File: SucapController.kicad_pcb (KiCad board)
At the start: 2 copper layers, 39.2 x 30.4 mm, 44 parts, among them J2 , J4 Conn_02x03_Counter_Clockwise, J5 Conn_02x03_Counter_Clockwise, J6 Conn_02x03_Counter_Clockwise, Q1 SI2301, U1 HX9193-33GB, U10 TL431, U2 HX9193, U3 W25Q32JVSS, U4 STM32H750VBT6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

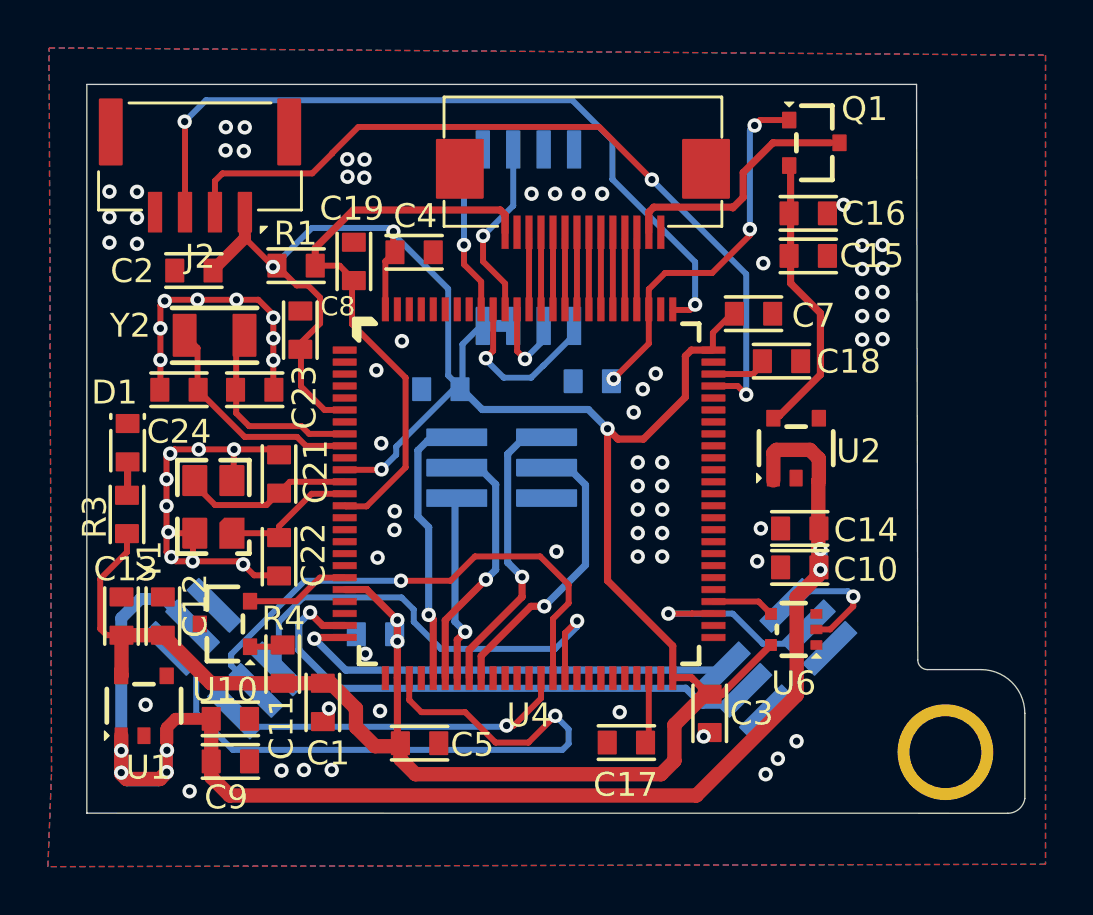
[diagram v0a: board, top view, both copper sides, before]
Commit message: fix some error of TL431
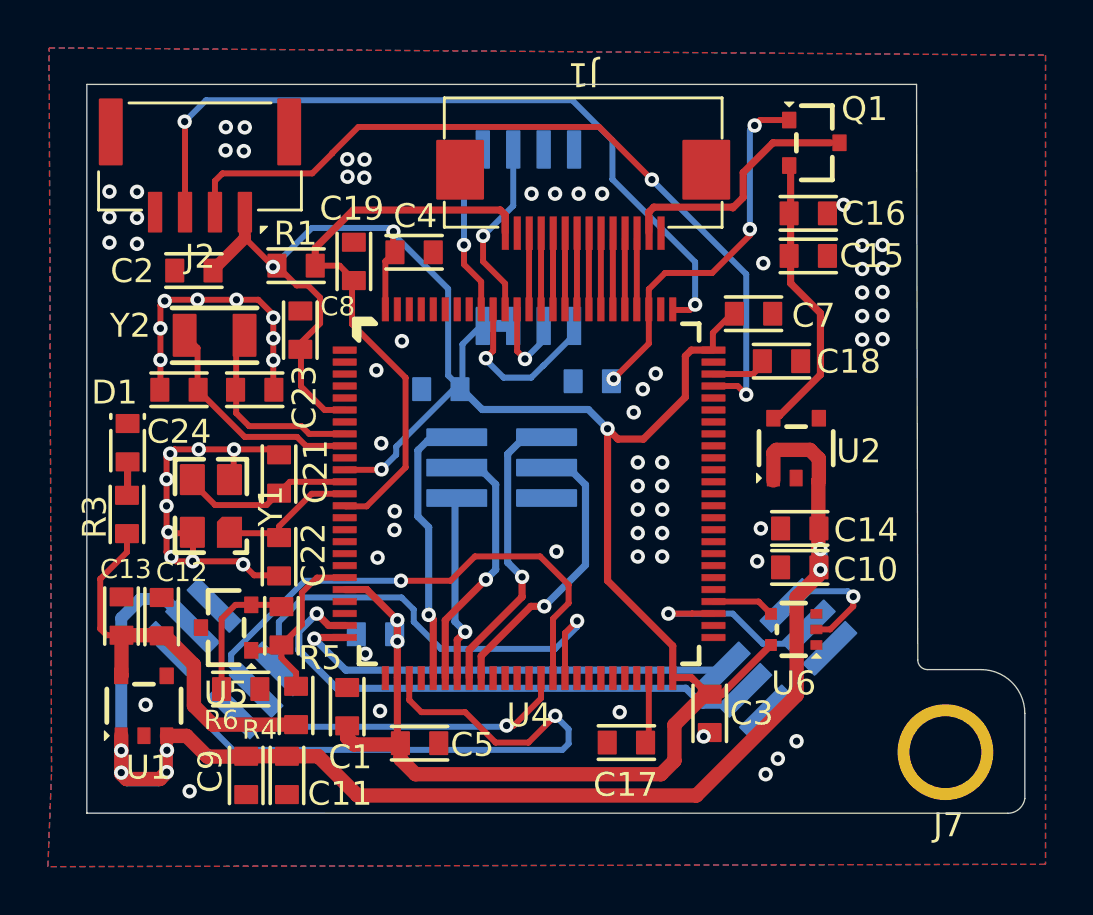
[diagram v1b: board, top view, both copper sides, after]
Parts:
- removed  : Conn_01x14, MECHANICAL_EDGE-CONN:FFC_14
- removed  : Screw_Terminal_01x01, GENERAL_HOLE:HOLE-04-03_1
- removed U10: TL431, GENERAL_SMALL-SEMI_SMD:SOT-23
- added J1: Conn_01x14, MECHANICAL_EDGE-CONN:FFC_14, F.Cu at (207.1, 86.1)
- added J7: Screw_Terminal_01x01, MECHANICAL:HOLE-04-03_1, F.Cu at (222.4, 110.7)
- added R5: 10k, GENERAL_RCL_SMD:R0603(1608M), F.Cu at (194.5, 105.5)
- added R6: 50k, GENERAL_RCL_SMD:R0603(1608M), F.Cu at (192.8, 108.1)
- added U5: TL431, GENERAL_SMALL-SEMI_SMD:SOT-23, F.Cu at (192.2, 105.5)
- R4: value Resistor -> 10k
- moved C11 3.34 mm to (194.7, 111.7), turned to 90 degrees
- moved R4 1.82 mm to (195.1, 108.8)
- moved C1 1.03 mm to (197.3, 108.8), turned to -90 degrees
- moved C9 0.88 mm to (193.0, 111.7), turned to 90 degrees
- moved Y1 0.11 mm to (191.6, 100.5)
- moved C12 0.06 mm to (189.5, 105.1)
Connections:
- R4 pad 2: Net-(R4-Pad2) -> /VREF
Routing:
- net Net-(R5-Pad1): track 0.00 -> 6.02 mm
- net /VREF: track 4.36 -> 7.92 mm
- net +5V: track 64.2 -> 62.0 mm
- net Net-(R4-Pad2): track 1.39 -> 0.00 mm
- net +3V3: track 119.2 -> 118.1 mm
- net GND: vias 82 -> 78

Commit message: fix some error
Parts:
-  : renamed from U5
-  : renamed from J2
-  : renamed from J1
-  : renamed from J7
-  : renamed from Y1
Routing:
- net +3V3: track 118.1 -> 120.2 mm
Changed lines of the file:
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@@
     (property "Sheetname" "")
     (attr smd)
-    (fp_text reference "U5" (at 0 2.75 unlocked) (layer "F.SilkS")
+    (fp_text reference " " (at 0 2.75 unlocked) (layer "F.SilkS")
       (effects (font (size 1 1) (thickness 0.15)))
     )
@@
     (property "Sheetname" "")
     (attr smd)
-    (fp_text reference "J2" (at 0 3.81 unlocked) (layer "F.SilkS")
+    (fp_text reference " " (at 0 3.81 unlocked) (layer "F.SilkS")
       (effects (font (size 1 1) (thickness 0.15)))
     )
@@
     (property "Sheetname" "")
     (attr smd)
-    (fp_text reference "J1" (at 0 3.683 180 unlocked) (layer "F.SilkS")
+    (fp_text reference " " (at 0 3.683 180 unlocked) (layer "F.SilkS")
       (effects (font (size 1 1) (thickness 0.15)))
     )
@@
     (property "Sheetname" "")
     (attr smd)
-    (fp_text reference "J7" (at 0 3.048 unlocked) (layer "F.SilkS")
+    (fp_text reference " " (at 0 3.048 unlocked) (layer "F.SilkS")
       (effects (font (size 1 1) (thickness 0.15)))
     )
@@
     (property "Sheetname" "")
     (attr smd)
-    (fp_text reference "Y1" (at 0 2.5 90 unlocked) (layer "F.SilkS")
+    (fp_text reference " " (at 0 2.5 90 unlocked) (layer "F.SilkS")
       (effects (font (size 1 1) (thickness 0.15)))
     )
@@
     (property "Sheetname" "")
     (attr smd)
-    (fp_text reference "R6" (at 0.8128 -1.2954) (layer "F.SilkS")
+    (fp_text reference "R6" (at 0.8128 -1.397) (layer "F.SilkS")
       (effects (font (size 0.8 0.8) (thickness 0.15)))
     )
@@
   (segment (start 212.2016 108.3184) (end 212.3948 108.3184) (width 0.6) (layer "F.Cu") (net 2))
   (segment (start 208.1276 97.2312) (end 208.561711 97.665311) (width 0.3) (layer "F.Cu") (net 2))
+  (segment (start 197.2056 109.5882) (end 197.2564 109.639) (width 0.6) (layer "F.Cu") (net 2))
   (segment (start 196.310994 96.449) (end 195.326 95.464006) (width 0.25) (layer "F.Cu") (net 2))
   (segment (start 199.479 110.363) (end 199.479 111.029) (width 0.6) (layer "F.Cu") (net 2))
@@
   (segment (start 199.479 111.029) (end 200.11 111.66) (width 0.6) (layer "F.Cu") (net 2))
   (segment (start 195.326 95.464006) (end 195.326 93.6374) (width 0.25) (layer "F.Cu") (net 2))
+  (segment (start 195.1228 109.5882) (end 197.2056 109.5882) (width 0.6) (layer "F.Cu") (net 2))
   (segment (start 187.2106 105.8544) (end 186.944 105.5878) (width 0.25) (layer "F.Cu") (net 2))
   (segment (start 198.671 98.949) (end 197.176 98.949) (width 0.25) (layer "F.Cu") (net 2))
   (segment (start 197.5358 110.4138) (end 199.4282 110.4138) (width 0.6) (layer "F.Cu") (net 2))
-  (segment (start 197.2056 109.5882) (end 197.2564 109.639) (width 0.6) (layer "F.Cu") (net 2))
   (segment (start 197.2564 110.1344) (end 197.5358 110.4138) (width 0.6) (layer "F.Cu") (net 2))
   (segment (start 199.4282 110.4138) (end 199.479 110.363) (width 0.6) (layer "F.Cu") (net 2))
@@
   (segment (start 214.2068 94.949) (end 214.617 94.5388) (width 0.25) (layer "F.Cu") (net 95))
   (segment (start 212.526 94.949) (end 214.2068 94.949) (width 0.25) (layer "F.Cu") (net 95))
-  (segment (start 213.33 87.98) (end 210.059419 87.98) (width 0.3) (layer "F.Cu") (net 96))
-  (segment (start 215.0364 85.2932) (end 213.7918 86.5378) (width 0.3) (layer "F.Cu") (net 96))
-  (segment (start 210.059419 87.98) (end 209.85 88.189419) (width 0.3) (layer "F.Cu") (net 96))
-  (segment (start 209.85 88.189419) (end 209.85 89.03) (width 0.3) (layer "F.Cu") (net 96))
-  (segment (start 213.36 88.01) (end 213.33 87.98) (width 0.3) (layer "F.Cu") (net 96))
-  (segment (start 213.7918 86.5378) (end 213.7918 87.5782) (width 0.3) (layer "F.Cu") (net 96))
-  (segment (start 217.4341 85.2932) (end 215.0364 85.2932) (width 0.3) (layer "F.Cu") (net 96))
-  (segment (start 213.7918 87.5782) (end 213.36 88.01) (width 0.3) (layer "F.Cu") (net 96))
-  (segment (start 194.4394 104.587) (end 194.5132 104.6608) (width 0.25) (layer "F.Cu") (net 98))
+  (segment (start 209.8616 88.2074) (end 210.0508 88.0182) (width 0.3) (layer "F.Cu") (net 96))
+  (segment (start 214.8586 85.2932) (end 217.8136 85.2932) (width 0.3) (layer "F.Cu") (net 96))
+  (segment (start 209.8616 89.0682) (end 209.8616 88.2074) (width 0.3) (layer "F.Cu") (net 96))
+  (segment (start 210.0508 88.0182) (end 213.367285 88.0182) (width 0.3) (layer "F.Cu") (net 96))
+  (segment (start 213.367285 88.0182) (end 214.8586 86.526885) (width 0.3) (layer "F.Cu") (net 96))
+  (segment (start 214.8586 86.526885) (end 214.8586 85.2932) (width 0.3) (layer "F.Cu") (net 96))
   (segment (start 193.2518 104.587) (end 194.4394 104.587) (width 0.25) (layer "F.Cu") (net 98))
   (segment (start 192.0114 105.1686) (end 192.593 104.587) (width 0.25) (layer "F.Cu") (net 98))
-  (segment (start 194.5894 104.737) (end 194.829 104.737) (width 0.25) (layer "F.Cu") (net 98))
   (segment (start 192.593 104.587) (end 193.2518 104.587) (width 0.25) (layer "F.Cu") (net 98))
   (segment (start 192.0114 108.1024) (end 192.0114 105.1686) (width 0.25) (layer "F.Cu") (net 98))
-  (segment (start 194.541 104.6886) (end 194.5894 104.737) (width 0.25) (layer "F.Cu") (net 98))
   (zone (net 0) (net_name "") (layers F&B.Cu) (hatch edge 0.508)
     (connect_pads (clearance 0))
